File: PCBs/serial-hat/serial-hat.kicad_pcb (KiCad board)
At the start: 2 copper layers, 65 x 56 mm, 14 parts, among them CN1 Modem port, CN2 Printer port, J1 Conn_01x02_Pin, J7 Rpi headers, U2 MAX3232

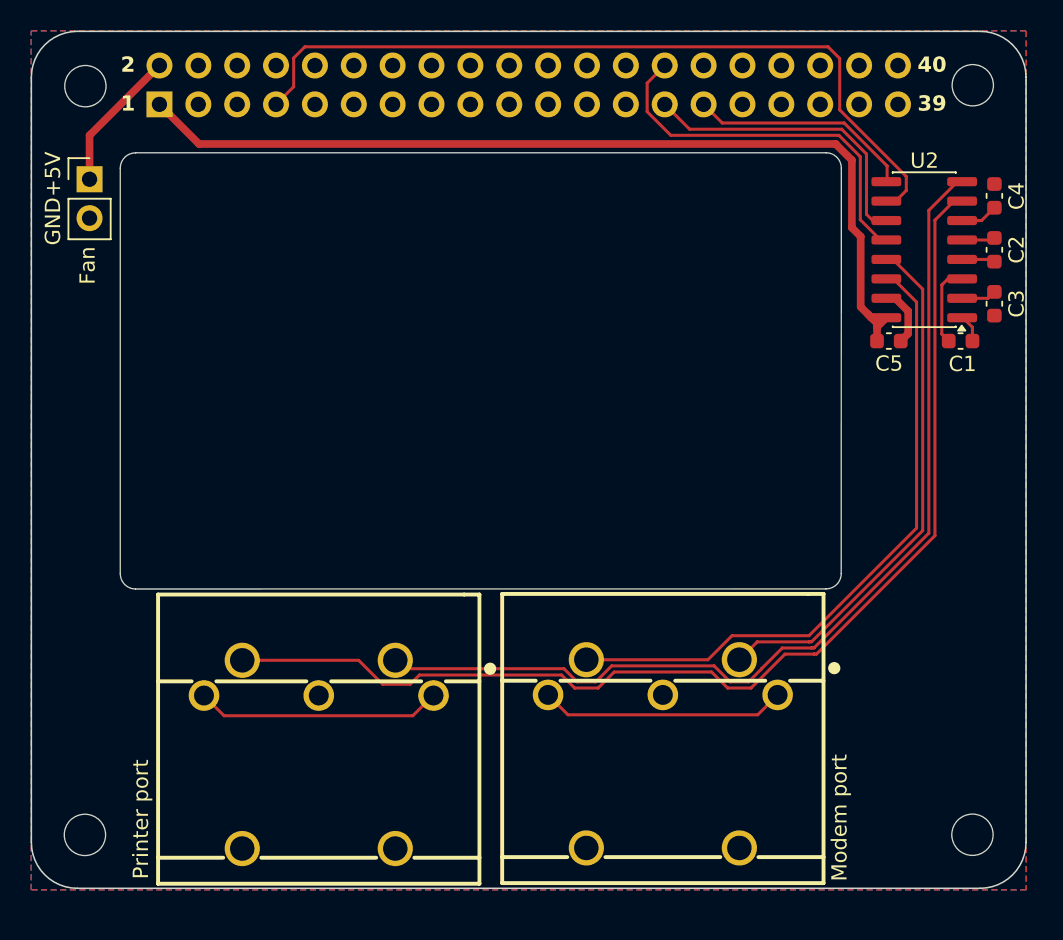
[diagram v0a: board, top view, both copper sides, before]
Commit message: Add gpio-fan ability
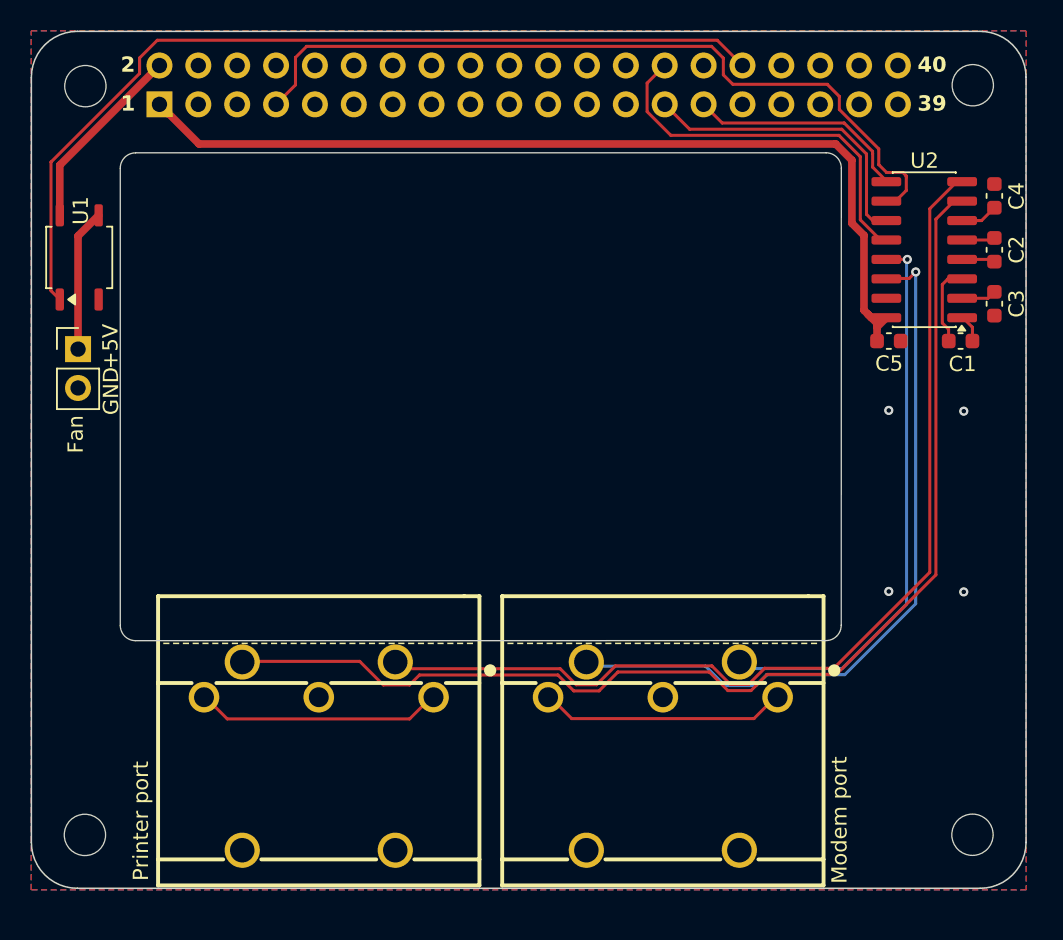
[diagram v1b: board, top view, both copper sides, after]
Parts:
- added U1: PC817C-S, Package_SO:SOP-4_3.8x4.1mm_P2.54mm, F.Cu at (125.8, 67.4)
- moved J1 11.1 mm to (125.7, 73.4)
- moved CN1 0.15 mm to (164.0, 100.0)
- moved CN2 0.11 mm to (141.5, 100.0)
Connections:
- J1 pad 1: 5V -> FAN_5V
- J7 pad 32: unconnected-(J7-Pin_32-Pad32) -> FAN_CTRL
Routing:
- net FAN_CTRL: track 0.00 -> 59.0 mm
- net FAN_5V: track 0.00 -> 9.30 mm
- net RX0_in: track 42.5 -> 48.2 mm, vias 0 -> 1
- net GND: track 3.93 -> 0.00 mm, vias 0 -> 4
- net 5V: track 9.33 -> 12.5 mm
- net TX0_in: track 34.4 -> 36.8 mm, vias 0 -> 1
- net RX1_in: track 74.5 -> 76.3 mm
- net TX1_in: track 64.4 -> 66.3 mm
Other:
- outline, holes or cut-outs redrawn
- board text added: "Apple II serial hat for Pi 4/5"
- board text added: "colino.net"
- board text removed: "Apple II serial hat for Pi 4/5 https://colino.net/"

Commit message: Update to new lib
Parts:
- CN1, CN2: footprint DIN5:CONN-TH_DIN-504-M10 -> Colins-Kicad:DIN-5-M C2939346
- U1: footprint Package_SO:SOP-4_3.8x4.1mm_P2.54mm -> Colins-Kicad:PC817C-S C3008369
- moved U1 2.11 mm to (125.7, 65.3)
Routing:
- net FAN_5V: track 9.30 -> 13.0 mm
- net FAN_CTRL: track 59.0 -> 62.5 mm
